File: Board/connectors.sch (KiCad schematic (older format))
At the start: 3 parts, among them J1 BATT+, J2 BATT-, J3 USB_A_Stacked

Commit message: Routing done.
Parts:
- added J4: Barrel_Jack_Switch, Connectors_custom:BarrelJack_712RA, symbol Connector:Barrel_Jack_Switch
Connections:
- net GND: now also J4.2
- new net +12V: J4.1
- no-connect marks 5 -> 6
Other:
- note added: "Barrel Jack 12V"
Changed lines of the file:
@@
 Wire Wire Line
 	2950 2600 3200 2600
+$Comp
+L Connector:Barrel_Jack_Switch J4
+U 1 1 5C4B0375
+P 9400 2350
+F 0 "J4" H 9455 2667 50  0000 C CNN
+F 1 "Barrel_Jack_Switch" H 9455 2576 50  0000 C CNN
+F 2 "Connectors_custom:BarrelJack_712RA" H 9450 2310 50  0001 C CNN
+F 3 "~" H 9450 2310 50  0001 C CNN
+	1    9400 2350
+	1    0    0    -1
+$EndComp
+Wire Wire Line
+	9700 2250 10100 2250
+Wire Wire Line
+	10100 2250 10100 2100
+$Comp
+L power:+12V #PWR06
+U 1 1 5C4B04CF
+P 10100 2100
+F 0 "#PWR06" H 10100 1950 50  0001 C CNN
+F 1 "+12V" H 10115 2273 50  0000 C CNN
+F 2 "" H 10100 2100 50  0001 C CNN
+F 3 "" H 10100 2100 50  0001 C CNN
+	1    10100 2100
+	1    0    0    -1
+$EndComp
+Wire Wire Line
+	9700 2450 10100 2450
+Wire Wire Line
+	10100 2450 10100 2600
+NoConn ~ 9700 2350
+$Comp
+L power:GND #PWR07
+U 1 1 5C4B0703
+P 10100 2600
+F 0 "#PWR07" H 10100 2350 50  0001 C CNN
+F 1 "GND" H 10105 2427 50  0000 C CNN
+F 2 "" H 10100 2600 50  0001 C CNN
+F 3 "" H 10100 2600 50  0001 C CNN
+	1    10100 2600
+	1    0    0    -1
+$EndComp
+Text Notes 8850 1600 0    118  ~ 24
+Barrel Jack 12V
 $EndSCHEMATC

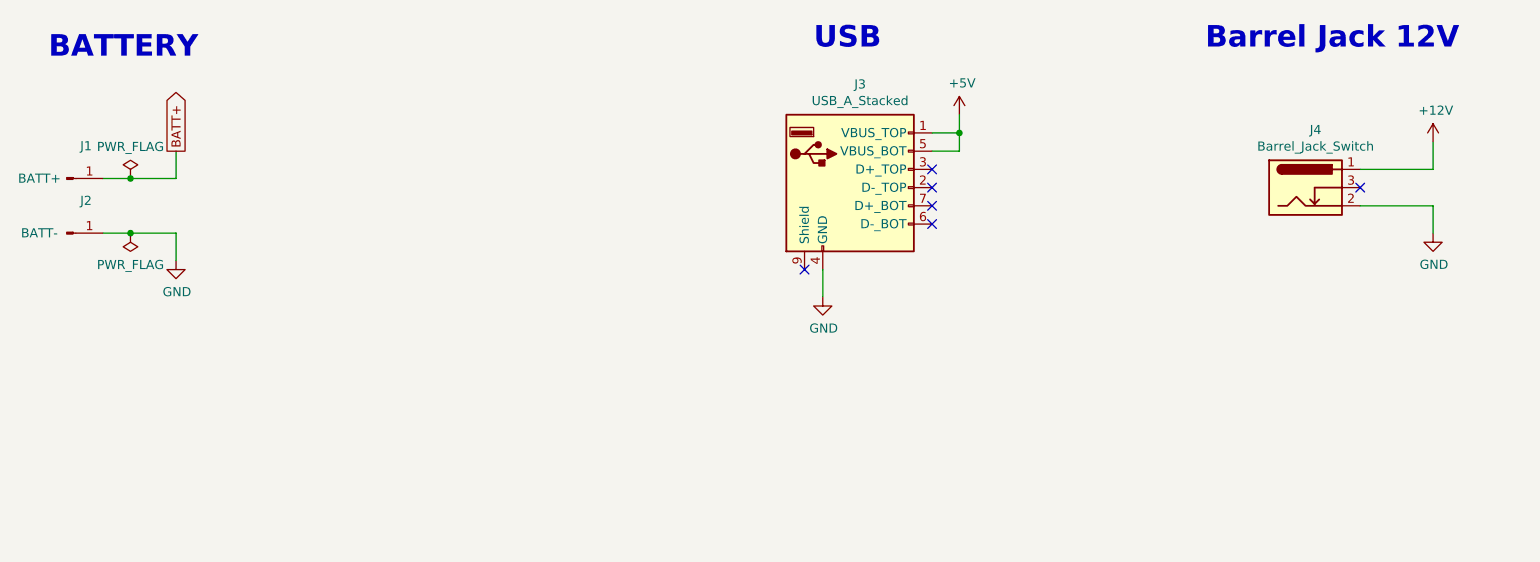
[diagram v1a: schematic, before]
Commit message: Routing done, waiting for mechanical integration.
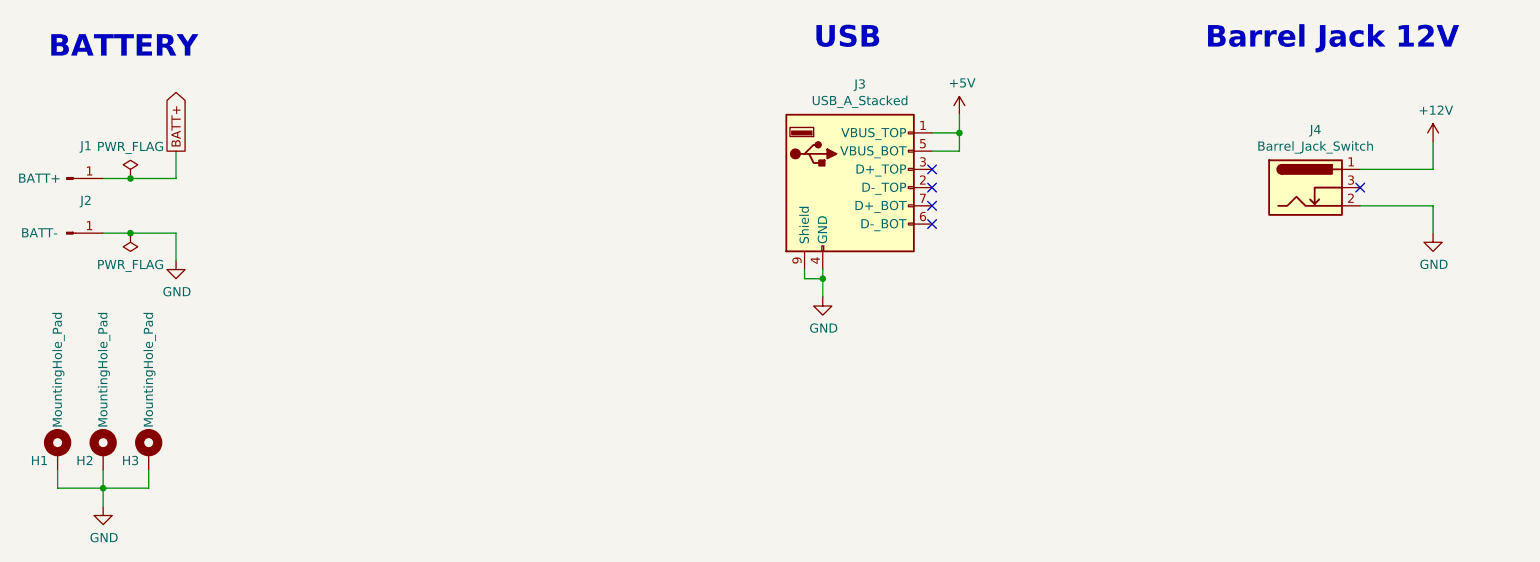
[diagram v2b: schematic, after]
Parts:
- added H1, H2, H3: MountingHole_Pad, MountingHole:MountingHole_2.2mm_M2_Pad_Via, symbol Mechanical:MountingHole_Pad
- J4: Farnell (none) -> 1608755; Ref (none) -> 712RA
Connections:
- net GND: now also J3.9 (Shield), H1.1, H2.1, H3.1
- no-connect marks 6 -> 5
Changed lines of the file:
@@
 $EndComp
 Wire Wire Line
-	6750 2800 6750 2950
-NoConn ~ 6650 2800
+	6750 2800 6750 2850
 NoConn ~ 7350 2550
 NoConn ~ 7350 2450
@@
 F 2 "Connectors_custom:BarrelJack_712RA" H 9450 2310 50  0001 C CNN
 F 3 "~" H 9450 2310 50  0001 C CNN
+F 4 "1608755" H 9400 2350 50  0001 C CNN "Farnell"
+F 5 "712RA" H 9400 2350 50  0001 C CNN "Ref"
 	1    9400 2350
 	1    0    0    -1
@@
 Text Notes 8850 1600 0    118  ~ 24
 Barrel Jack 12V
+$Comp
+L Mechanical:MountingHole_Pad H1
+U 1 1 5C55F291
+P 2550 3800
+F 0 "H1" H 2450 3750 50  0000 C CNN
+F 1 "MountingHole_Pad" V 2550 4250 50  0000 C CNN
+F 2 "MountingHole:MountingHole_2.2mm_M2_Pad_Via" H 2550 3800 50  0001 C CNN
+F 3 "~" H 2550 3800 50  0001 C CNN
+	1    2550 3800
+	1    0    0    -1
+$EndComp
+Wire Wire Line
+	2550 3900 2550 4000
+Wire Wire Line
+	2550 4000 2800 4000
+Wire Wire Line
+	2800 3900 2800 4000
+Connection ~ 2800 4000
+Wire Wire Line
+	3050 3900 3050 4000
+$Comp
+L power:GND #PWR08
+U 1 1 5C56099E
+P 2800 4100
+F 0 "#PWR08" H 2800 3850 50  0001 C CNN
+F 1 "GND" H 2805 3927 50  0000 C CNN
+F 2 "" H 2800 4100 50  0001 C CNN
+F 3 "" H 2800 4100 50  0001 C CNN
+	1    2800 4100
+	1    0    0    -1
+$EndComp
+$Comp
+L Mechanical:MountingHole_Pad H2
+U 1 1 5C5609F4
+P 2800 3800
+F 0 "H2" H 2700 3750 50  0000 C CNN
+F 1 "MountingHole_Pad" V 2800 4250 50  0000 C CNN
+F 2 "MountingHole:MountingHole_2.2mm_M2_Pad_Via" H 2800 3800 50  0001 C CNN
+F 3 "~" H 2800 3800 50  0001 C CNN
+	1    2800 3800
+	1    0    0    -1
+$EndComp
+$Comp
+L Mechanical:MountingHole_Pad H3
+U 1 1 5C560A1A
+P 3050 3800
+F 0 "H3" H 2950 3750 50  0000 C CNN
+F 1 "MountingHole_Pad" V 3050 4250 50  0000 C CNN
+F 2 "MountingHole:MountingHole_2.2mm_M2_Pad_Via" H 3050 3800 50  0001 C CNN
+F 3 "~" H 3050 3800 50  0001 C CNN
+	1    3050 3800
+	1    0    0    -1
+$EndComp
+Wire Wire Line
+	6650 2800 6650 2850
+Wire Wire Line
+	6650 2850 6750 2850
+Connection ~ 6750 2850
+Wire Wire Line
+	6750 2850 6750 2950
+Wire Wire Line
+	2800 4000 3050 4000
+Wire Wire Line
+	2800 4000 2800 4100
 $EndSCHEMATC
